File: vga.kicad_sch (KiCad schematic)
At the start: 0 parts

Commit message: add notes for other ports
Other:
- note added: "VGA output (binary 4 bit, or higher order with oversampling?) Composite video and audio? 3.5mm audio jack?"
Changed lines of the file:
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@@
 (kicad_sch (version 20211123) (generator eeschema)
   (paper "A4")
+  (text "VGA output (binary 4 bit, or higher order with oversampling?)\nComposite video and audio?\n3.5mm audio jack?"
+    (at 124.46 91.44 0)
+    (effects (font (size 1.27 1.27)) (justify left bottom))
+  )
 )

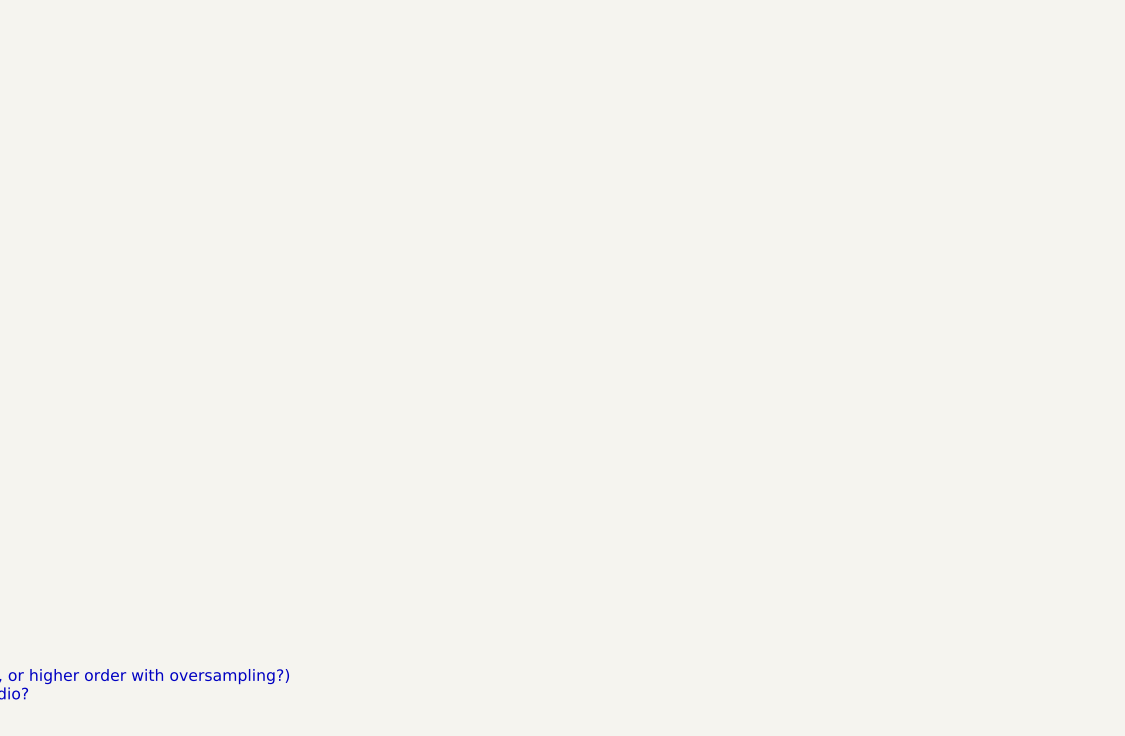
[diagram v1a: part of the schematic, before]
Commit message: add VGA connector and resistor DACs
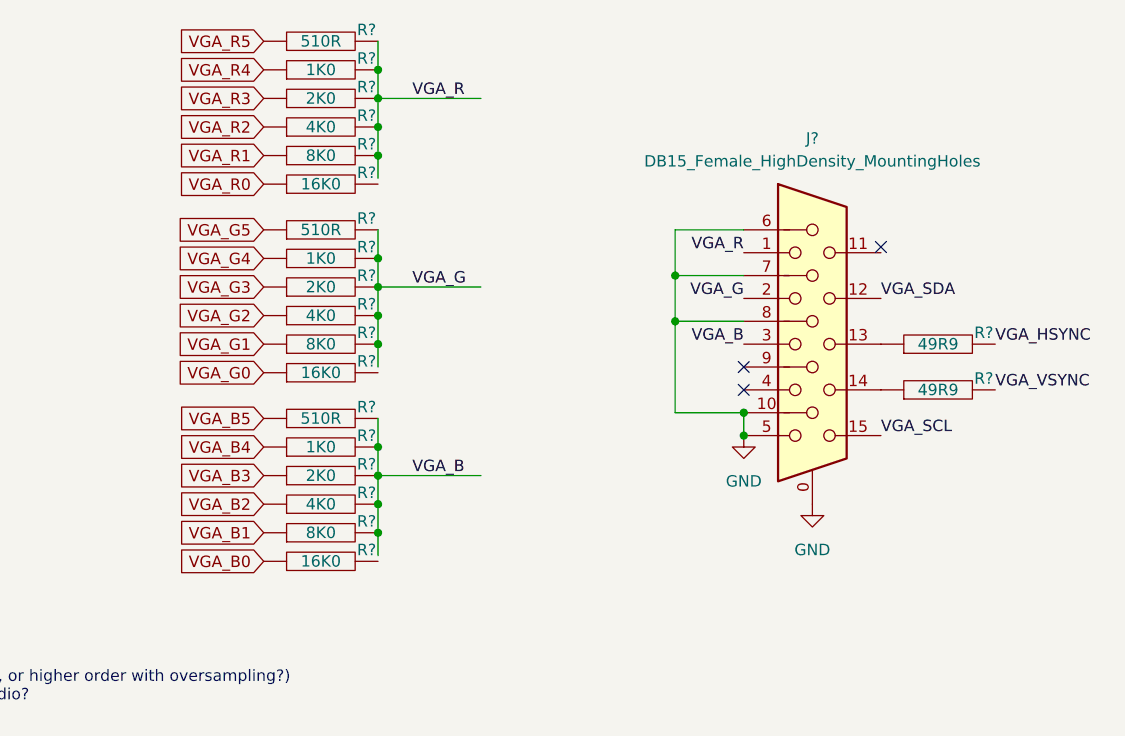
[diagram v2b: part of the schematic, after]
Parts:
- added J?: DB15_Female_HighDensity_MountingHoles, Connector_Dsub:DSUB-15-HD_Female_Horizontal_P2.29x1.98mm_EdgePinOffset8.35mm_Housed_MountingHolesOffset10.89mm, symbol Connector:DB15_Female_HighDensity_MountingHoles
- added R? (x2): 49R9, Resistor_THT:R_Box_L8.4mm_W2.5mm_P5.08mm, symbol pspice:R
- added R? (x3): 16K0, Resistor_THT:R_Box_L8.4mm_W2.5mm_P5.08mm, symbol pspice:R
- added R? (x3): 2K0, Resistor_THT:R_Box_L8.4mm_W2.5mm_P5.08mm, symbol pspice:R
- added R? (x3): 510R, Resistor_THT:R_Box_L8.4mm_W2.5mm_P5.08mm, symbol pspice:R
- added R? (x3): 4K0, Resistor_THT:R_Box_L8.4mm_W2.5mm_P5.08mm, symbol pspice:R
- added R? (x3): 1K0, Resistor_THT:R_Box_L8.4mm_W2.5mm_P5.08mm, symbol pspice:R
- added R? (x3): 8K0, Resistor_THT:R_Box_L8.4mm_W2.5mm_P5.08mm, symbol pspice:R
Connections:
- new net: J?.13, R?.1
- new net: J?.14, R?.1
- new net GND: J?.0, J?.10, J?.5, J?.6, J?.7, J?.8
- new net VGA_B: J?.3, R?.2, R?.2, R?.2, R?.2, R?.2
- new net VGA_B0: R?.1
- new net VGA_B1: R?.1
- new net VGA_B2: R?.1
- new net VGA_B3: R?.1
- new net VGA_B4: R?.1
- new net VGA_B5: R?.1
- new net VGA_G: J?.2, R?.2, R?.2, R?.2, R?.2, R?.2
- new net VGA_G0: R?.1
- new net VGA_G1: R?.1
- new net VGA_G2: R?.1
- new net VGA_G3: R?.1
- new net VGA_G4: R?.1
- new net VGA_G5: R?.1
- new net VGA_HSYNC: R?.2
- new net VGA_R: J?.1, R?.2, R?.2, R?.2, R?.2, R?.2
- new net VGA_R0: R?.1
- new net VGA_R1: R?.1
- new net VGA_R2: R?.1
- new net VGA_R3: R?.1
- new net VGA_R4: R?.1
- new net VGA_R5: R?.1
- new net VGA_SCL: J?.15
- new net VGA_SDA: J?.12
- new net VGA_VSYNC: R?.2
- no-connect marks 0 -> 3

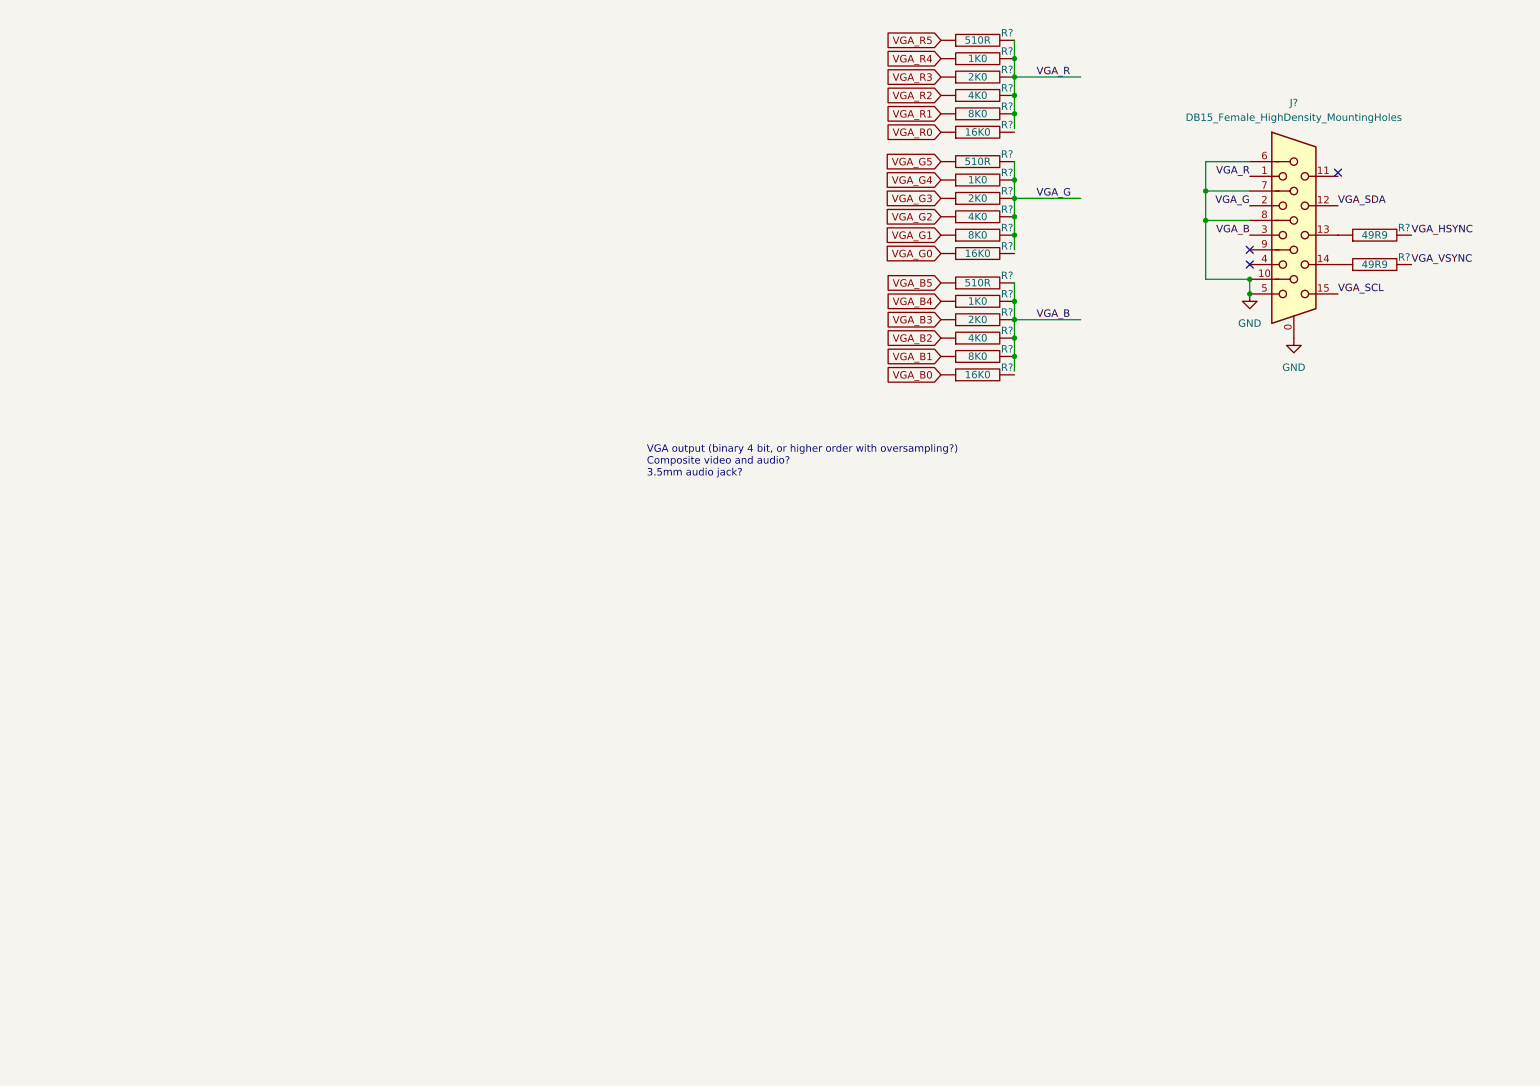
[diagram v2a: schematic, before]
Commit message: add resistor laddars for 3.5mm audio and component video outputs
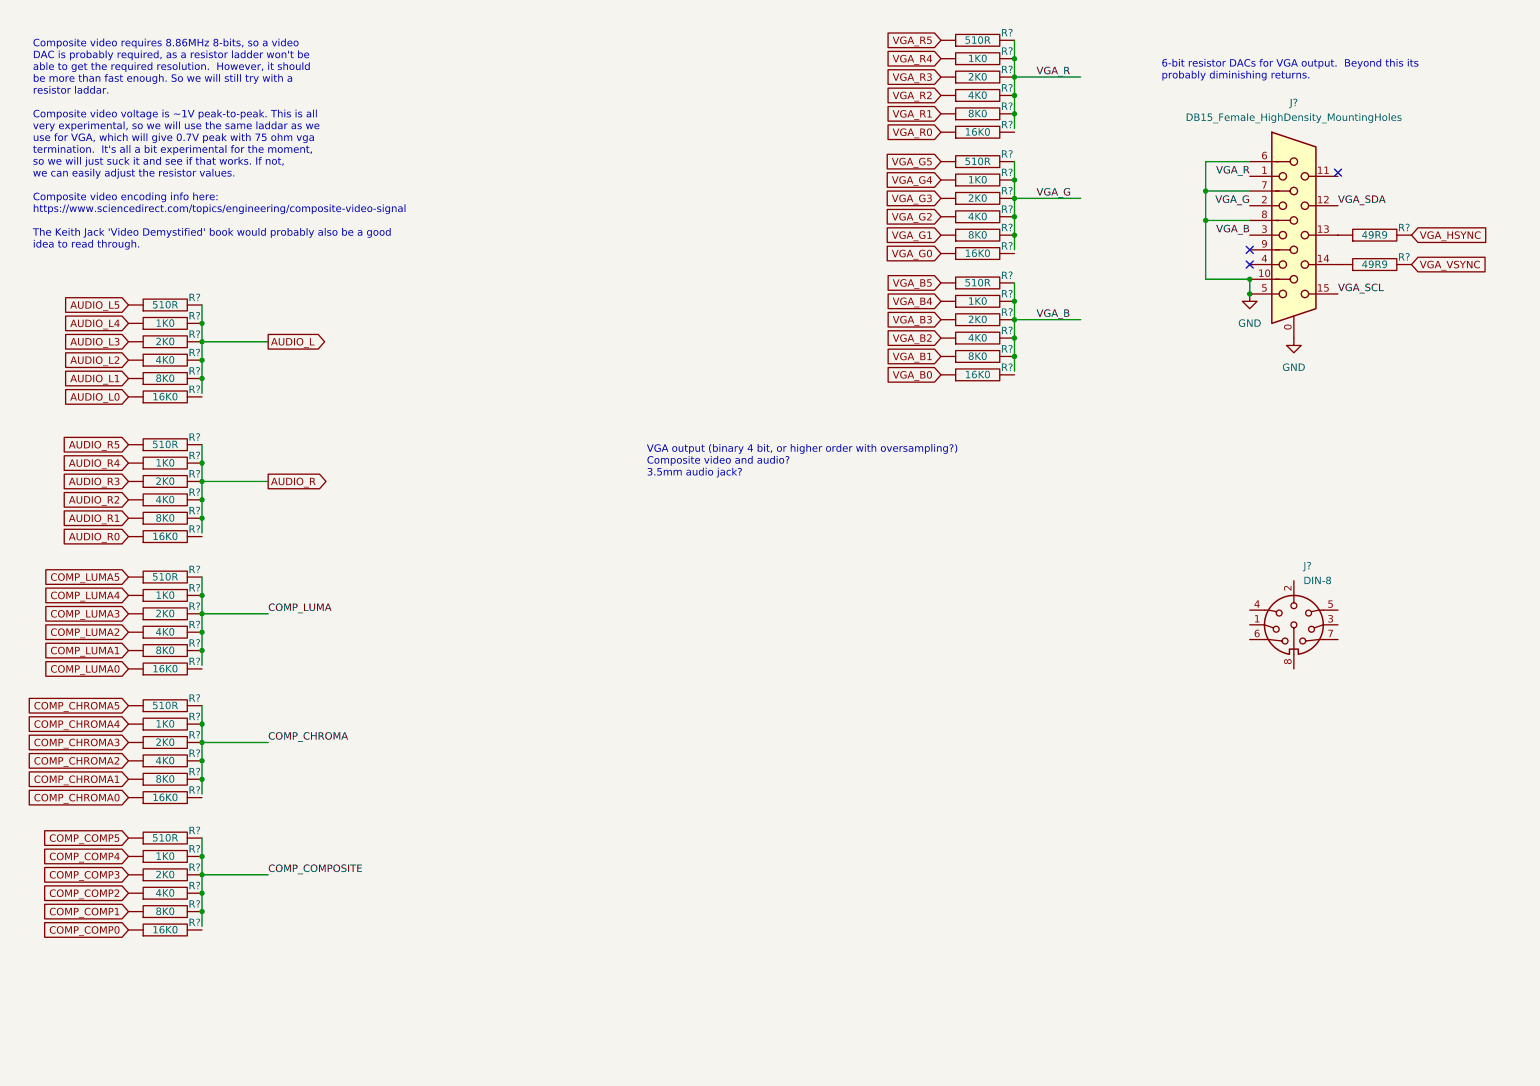
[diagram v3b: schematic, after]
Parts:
- added J?: DIN-8, symbol Connector:DIN-8
- added R? (x5): 510R, Resistor_THT:R_Box_L8.4mm_W2.5mm_P5.08mm, symbol pspice:R
- added R? (x5): 8K0, Resistor_THT:R_Box_L8.4mm_W2.5mm_P5.08mm, symbol pspice:R
- added R? (x5): 2K0, Resistor_THT:R_Box_L8.4mm_W2.5mm_P5.08mm, symbol pspice:R
- added R? (x5): 1K0, Resistor_THT:R_Box_L8.4mm_W2.5mm_P5.08mm, symbol pspice:R
- added R? (x5): 16K0, Resistor_THT:R_Box_L8.4mm_W2.5mm_P5.08mm, symbol pspice:R
- added R? (x5): 4K0, Resistor_THT:R_Box_L8.4mm_W2.5mm_P5.08mm, symbol pspice:R
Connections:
- new net AUDIO_L: R?.2, R?.2, R?.2, R?.2, R?.2
- new net AUDIO_L0: R?.1
- new net AUDIO_L1: R?.1
- new net AUDIO_L2: R?.1
- new net AUDIO_L3: R?.1
- new net AUDIO_L4: R?.1
- new net AUDIO_L5: R?.1
- new net AUDIO_R: R?.2, R?.2, R?.2, R?.2, R?.2
- new net AUDIO_R0: R?.1
- new net AUDIO_R1: R?.1
- new net AUDIO_R2: R?.1
- new net AUDIO_R3: R?.1
- new net AUDIO_R4: R?.1
- new net AUDIO_R5: R?.1
- new net COMP_CHROMA: R?.2, R?.2, R?.2, R?.2, R?.2
- new net COMP_CHROMA0: R?.1
- new net COMP_CHROMA1: R?.1
- new net COMP_CHROMA2: R?.1
- new net COMP_CHROMA3: R?.1
- new net COMP_CHROMA4: R?.1
- new net COMP_CHROMA5: R?.1
- new net COMP_COMP0: R?.1
- new net COMP_COMP1: R?.1
- new net COMP_COMP2: R?.1
- new net COMP_COMP3: R?.1
- new net COMP_COMP4: R?.1
- new net COMP_COMP5: R?.1
- new net COMP_COMPOSITE: R?.2, R?.2, R?.2, R?.2, R?.2
- new net COMP_LUMA: R?.2, R?.2, R?.2, R?.2, R?.2
- new net COMP_LUMA0: R?.1
- new net COMP_LUMA1: R?.1
- new net COMP_LUMA2: R?.1
- new net COMP_LUMA3: R?.1
- new net COMP_LUMA4: R?.1
- new net COMP_LUMA5: R?.1
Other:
- note added: "6-bit resistor DACs for VGA output. Beyond this its probably diminishing returns."
- note added: "Composite video requires 8.86MHz 8-bits, so a video DAC is probably required, as a resistor ladder won't be able to get the required resolution. However, it should be more than fast enough. So we will still try with a resistor laddar. Composite video voltage is ~1V peak-to-peak. This is all very experimental, so we will use the same laddar as we use for VGA, which will give 0.7V peak with 75 ohm 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"

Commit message: add C64 A/V port
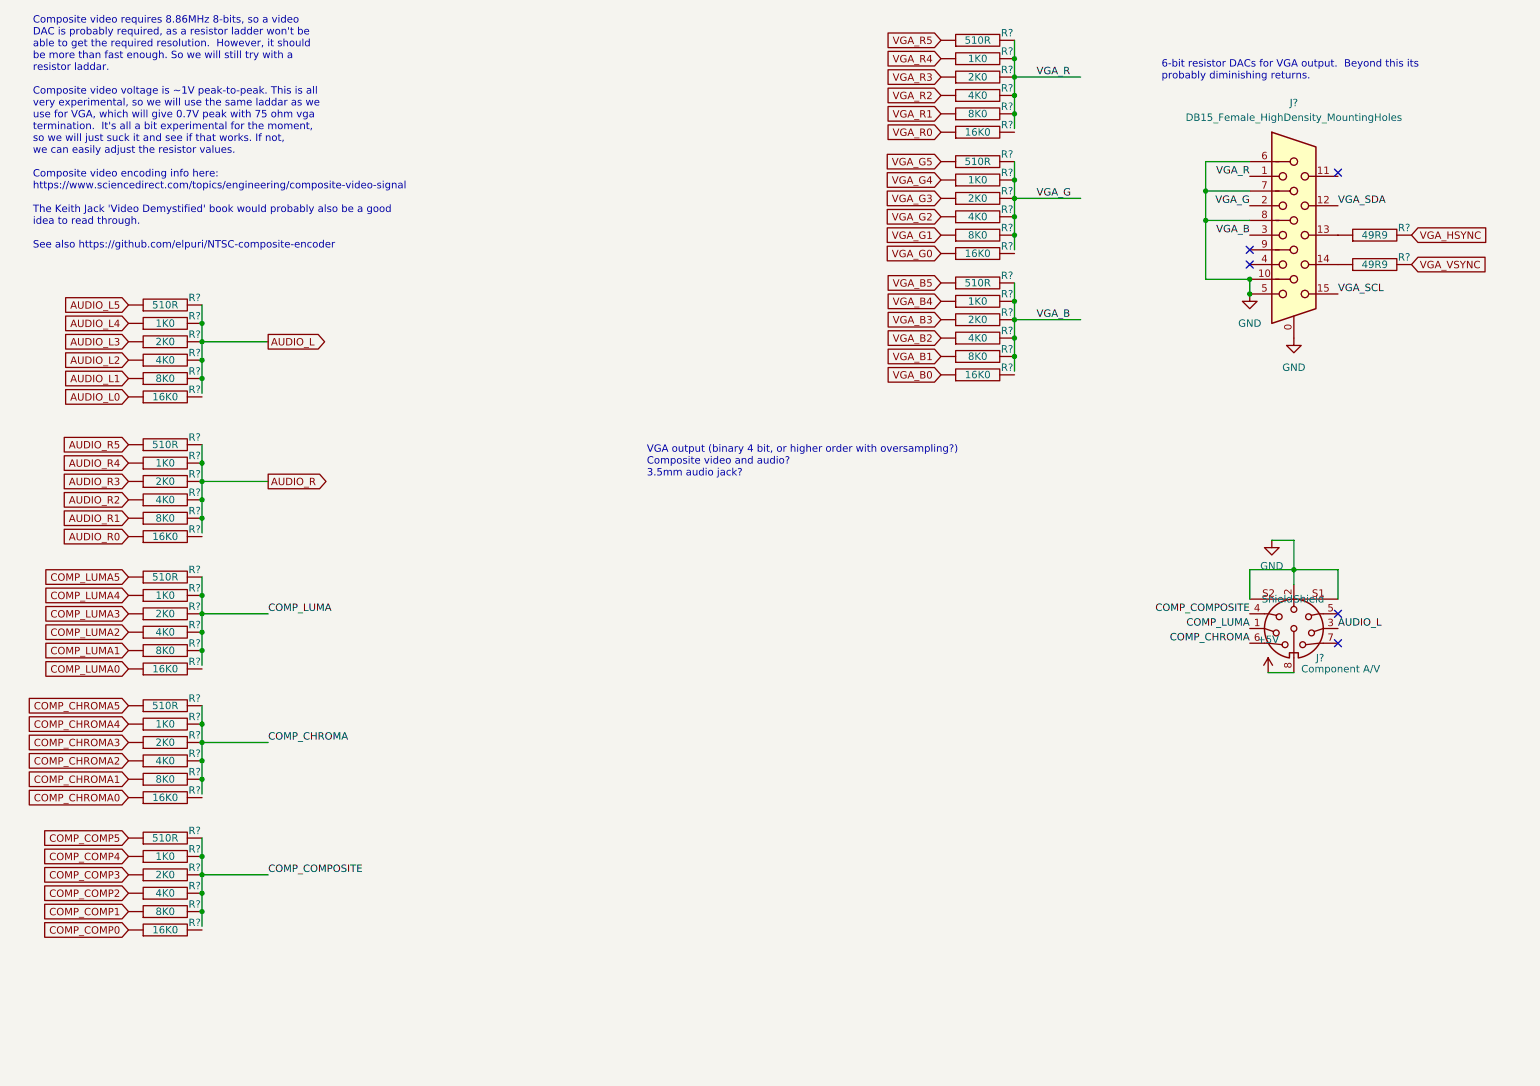
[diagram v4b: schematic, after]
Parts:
- removed J?: DIN-8, symbol Connector:DIN-8
- added J?: Component A/V, snapeda:CUI_SDF-80J, symbol 00Project-SDF-60J:SDF-80J
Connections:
- net AUDIO_L: now also J?.3
- net COMP_CHROMA: now also J?.6
- net COMP_COMPOSITE: now also J?.4
- net COMP_LUMA: now also J?.1
- net GND: now also J?.2, J?.S1 (Shield), J?.S2 (Shield)
- new net +5V: J?.8
- no-connect marks 3 -> 5
